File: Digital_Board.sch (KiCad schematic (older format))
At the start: 0 parts

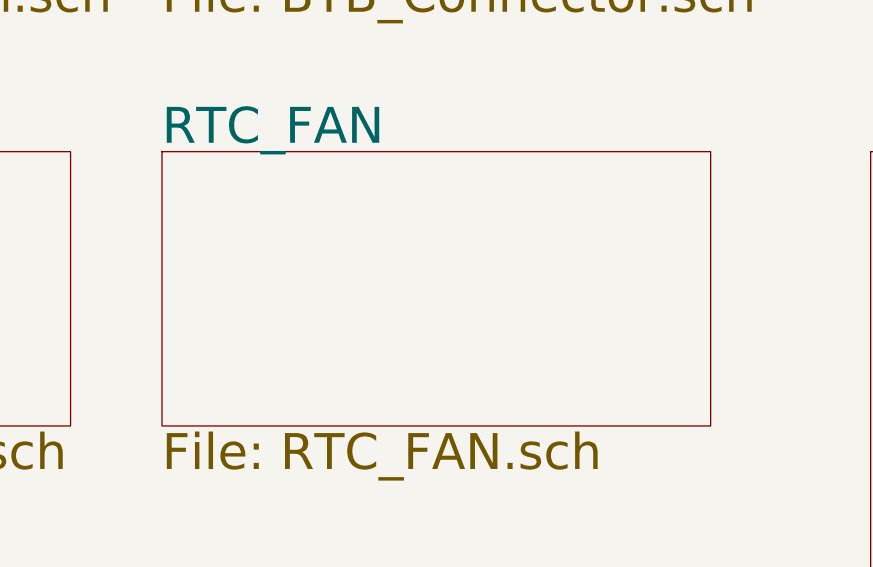
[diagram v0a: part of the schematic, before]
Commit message: Added new sheet for Ethernet PHY Connector and drawn schematic (continue)
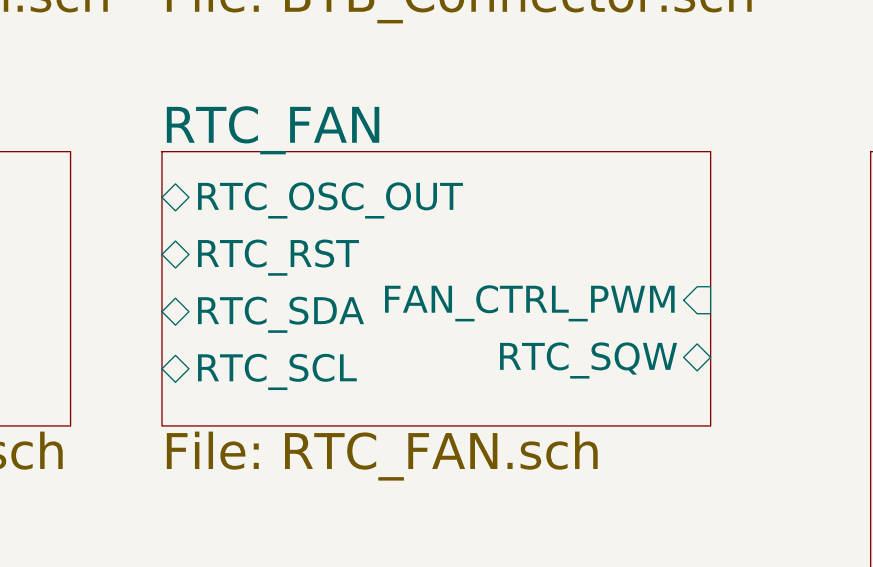
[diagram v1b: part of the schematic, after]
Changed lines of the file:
@@
 $Descr A2 23386 16535
 encoding utf-8
-Sheet 1 14
+Sheet 1 15
 Title "CGMPCX1006"
 Date "2021-02-03"
@@
 F0 "RTC_FAN" 157
 F1 "RTC_FAN.sch" 157
+F2 "RTC_SCL" B L 13900 4650 118
+F3 "RTC_SDA" B L 13900 4400 118
+F4 "RTC_RST" B L 13900 4150 118
+F5 "RTC_OSC_OUT" B L 13900 3900 118
+F6 "RTC_SQW" B R 16300 4600 118
+F7 "FAN_CTRL_PWM" I R 16300 4350 118
 $EndSheet
 $Sheet

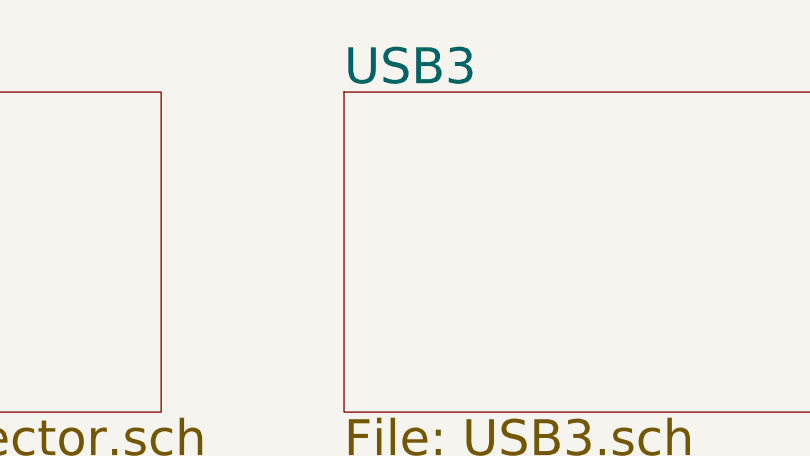
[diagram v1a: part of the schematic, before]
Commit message: Added USB SRAM sheet,Added USB3 ethernet ic
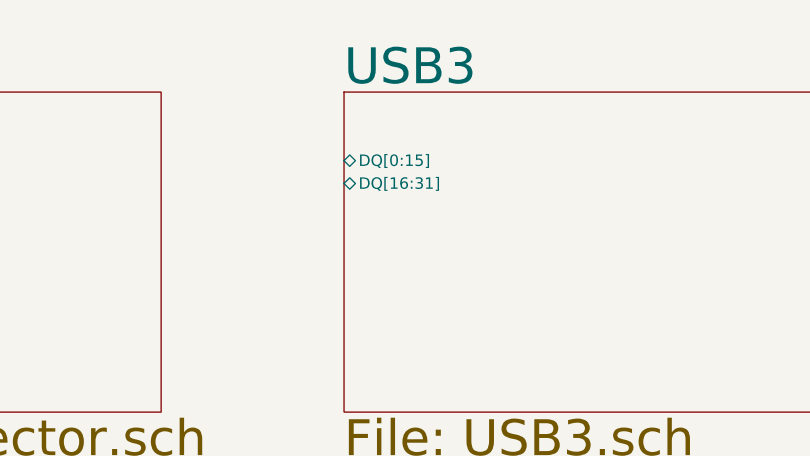
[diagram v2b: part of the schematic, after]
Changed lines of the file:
@@
 $Descr A2 23386 16535
 encoding utf-8
-Sheet 1 15
+Sheet 1 17
 Title "CGMPCX1006"
 Date "2021-02-03"
@@
 F0 "USB3" 157
 F1 "USB3.sch" 157
+F2 "DQ[0:15]" B L 17100 1800 50
+F3 "DQ[16:31]" B L 17100 1900 50
 $EndSheet
 $Sheet

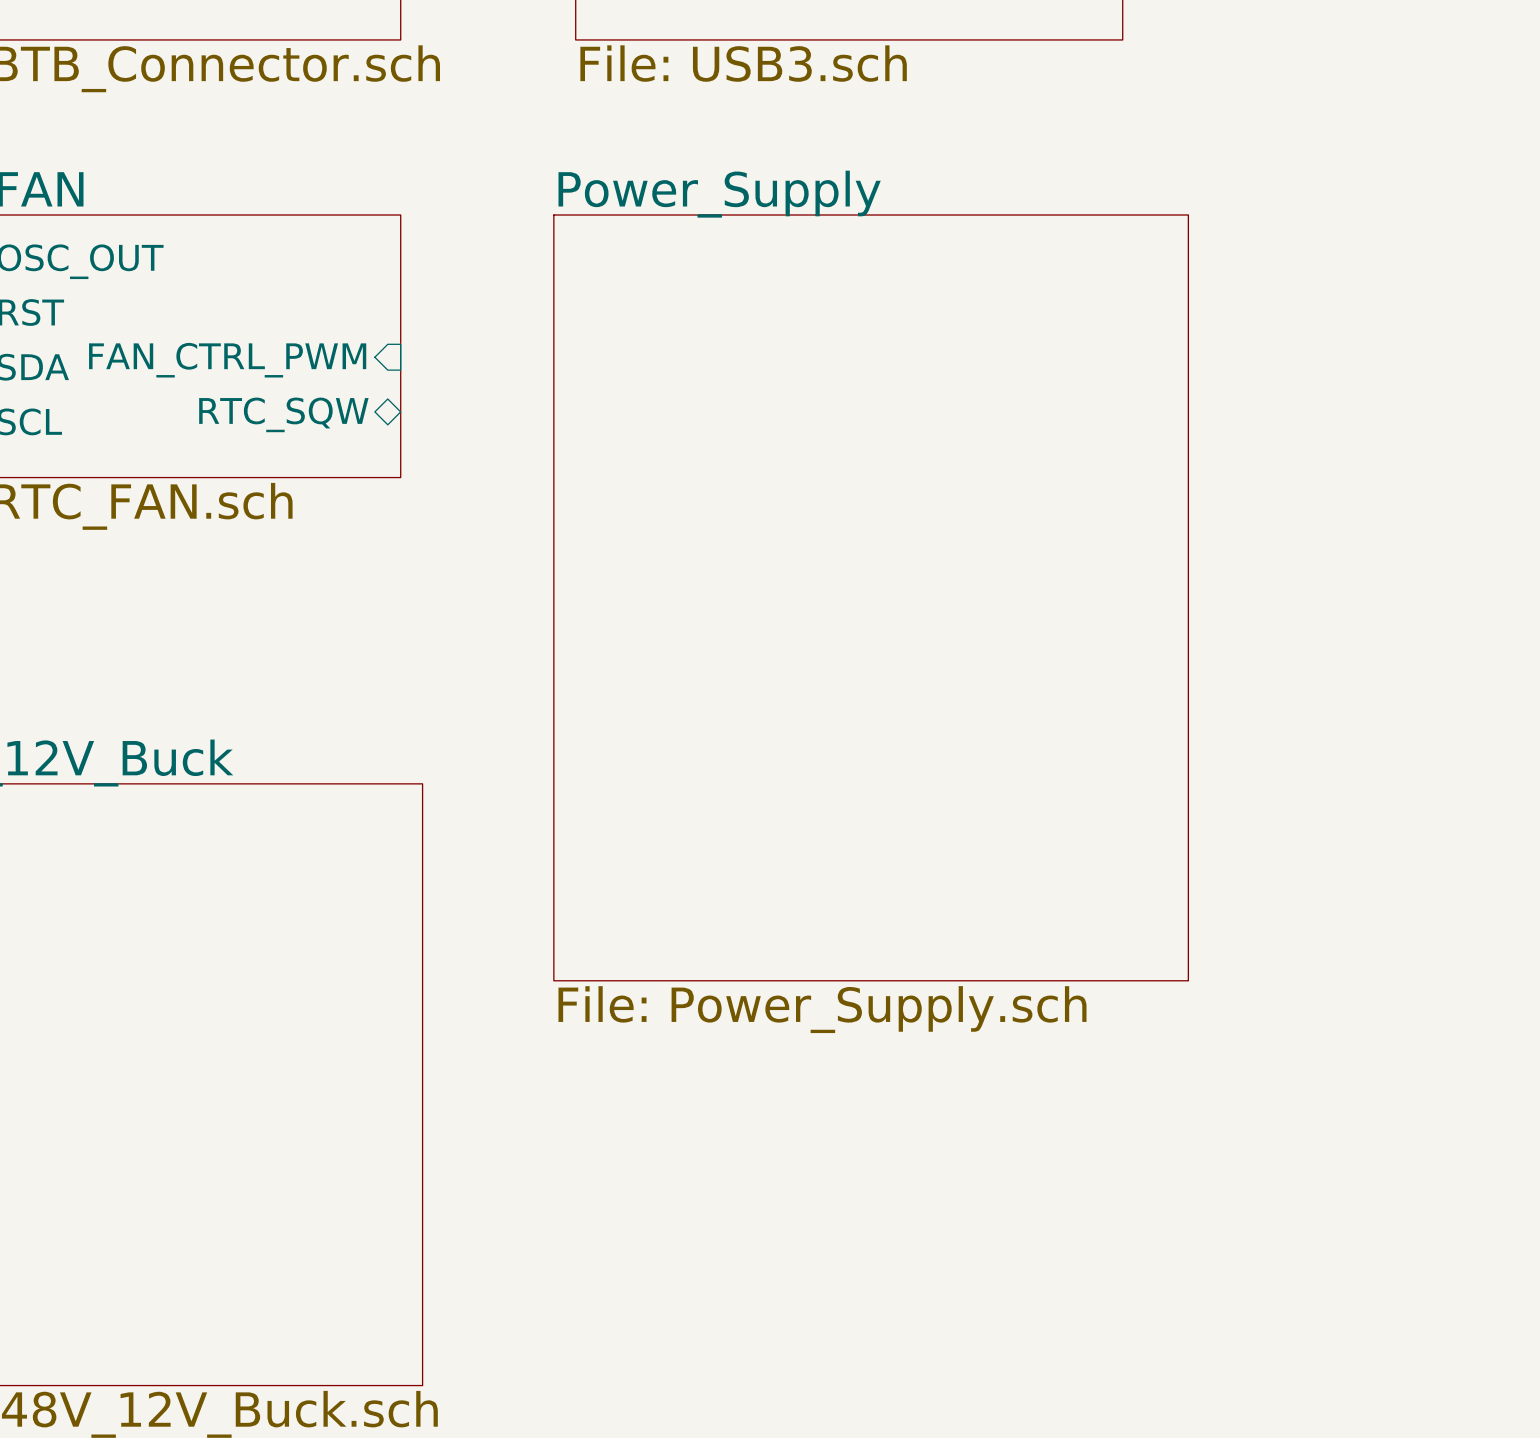
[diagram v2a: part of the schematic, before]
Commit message: Completed power 48v to 12v sheet
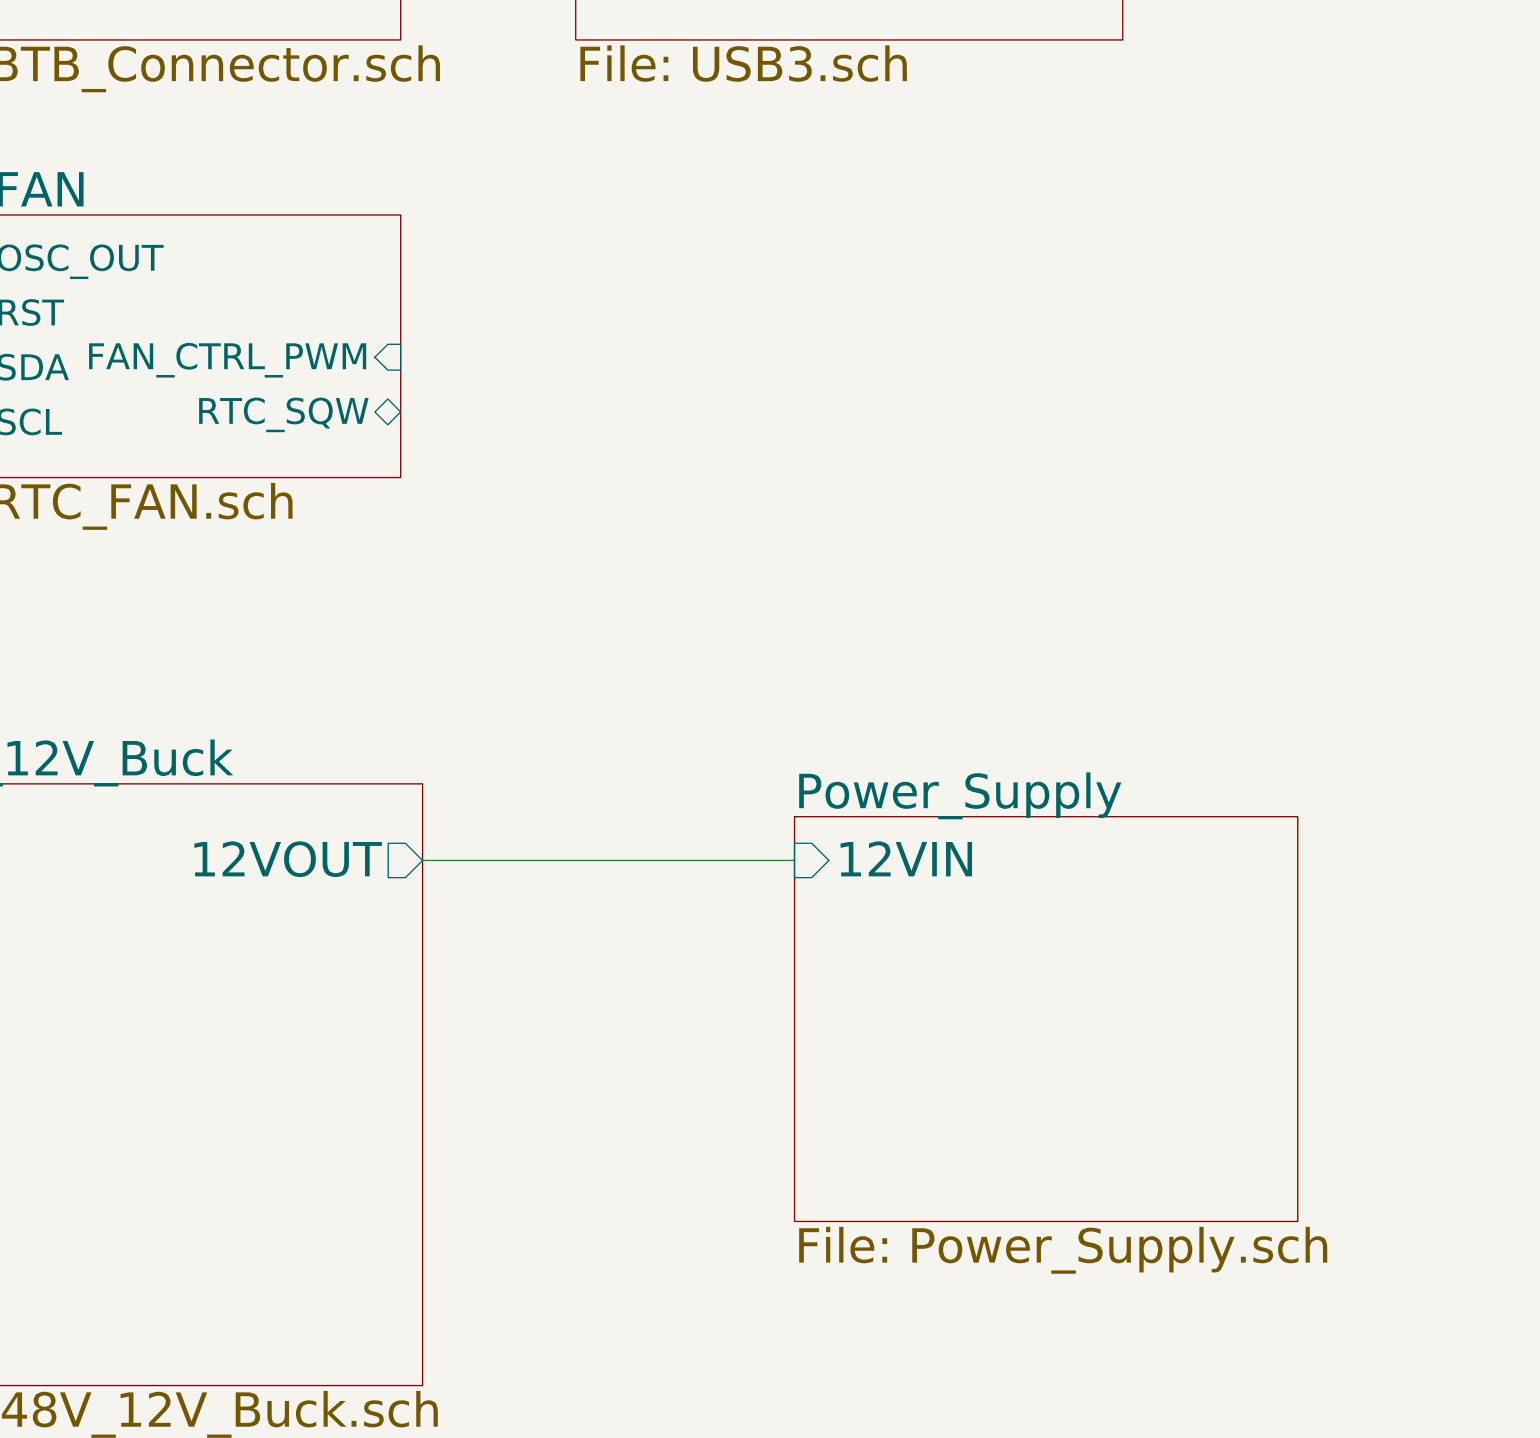
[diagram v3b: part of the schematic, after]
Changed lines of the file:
@@
 $EndSheet
 $Sheet
-S 17000 3700 2900 3500
+S 18100 6450 2300 1850
 U 601DF0A6
 F0 "Power_Supply" 157
 F1 "Power_Supply.sch" 157
+F2 "12VIN" I L 18100 6650 157
 $EndSheet
 $Sheet
@@
 F0 "48V_12V_Buck" 157
 F1 "48V_12V_Buck.sch" 157
+F2 "12VOUT" O R 16400 6650 157
 $EndSheet
+Wire Wire Line
+	16400 6650 18100 6650
 $EndSCHEMATC

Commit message: Completed USB3 1.2V Added 5V regulator cct partially completed Added BTB connector
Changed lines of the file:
@@
 $Descr A2 23386 16535
 encoding utf-8
-Sheet 1 17
+Sheet 1 18
 Title "CGMPCX1006"
 Date "2021-02-03"
@@
 $EndSheet
 $Sheet
-S 18100 6450 2300 1850
+S 5850 12700 2600 750
 U 601DF0A6
 F0 "Power_Supply" 157
 F1 "Power_Supply.sch" 157
-F2 "12VIN" I L 18100 6650 157
+F2 "12VIN" I L 5850 12900 157
 $EndSheet
 $Sheet
-S 13950 6300 2450 2750
+S 1750 12550 2450 900
 U 60256C5F
 F0 "48V_12V_Buck" 157
 F1 "48V_12V_Buck.sch" 157
-F2 "12VOUT" O R 16400 6650 157
+F2 "12VOUT" O R 4200 12900 157
 $EndSheet
 Wire Wire Line
-	16400 6650 18100 6650
+	4200 12900 5850 12900
+$Sheet
+S 2550 5850 2750 1550
+U 60318A5B
+F0 "BNC_trigger" 157
+F1 "BNC_Trigger.sch" 157
+$EndSheet
 $EndSCHEMATC

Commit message: Added sheet Ext_Analog
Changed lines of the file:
@@
-$EndSheet
-$Sheet
-S 17100 1500 2500 1400
-U 601E7BBE
-F0 "USB3" 157
-F1 "USB3.sch" 157
-F2 "DQ[0:15]" B L 17100 1800 50
-F3 "DQ[16:31]" B L 17100 1900 50
 $EndSheet
 $Sheet
@@
 $EndSheet
 $Sheet
-S 5500 3700 2800 1200
+S 17250 12000 2800 1200
 U 601E7C1E
 F0 "Comm_Interface" 157
@@
 $EndSheet
 $Sheet
-S 8800 3700 2300 1200
+S 17250 9950 2300 1200
 U 601E7C5A
 F0 "EEPROM" 157
@@
 $EndSheet
 $Sheet
-S 11600 3700 1900 1200
+S 17250 8150 1900 1200
 U 601E7C92
 F0 "Ethernet" 157
@@
 $EndSheet
 $Sheet
-S 13900 3700 2400 1200
+S 17100 4050 2400 1200
 U 601E7CC8
 F0 "RTC_FAN" 157
 F1 "RTC_FAN.sch" 157
-F2 "RTC_SCL" B L 13900 4650 118
-F3 "RTC_SDA" B L 13900 4400 118
-F4 "RTC_RST" B L 13900 4150 118
-F5 "RTC_OSC_OUT" B L 13900 3900 118
-F6 "RTC_SQW" B R 16300 4600 118
-F7 "FAN_CTRL_PWM" I R 16300 4350 118
+F2 "RTC_SCL" B L 17100 5000 118
+F3 "RTC_SDA" B L 17100 4750 118
+F4 "RTC_RST" B L 17100 4500 118
+F5 "RTC_OSC_OUT" B L 17100 4250 118
+F6 "RTC_SQW" B R 19500 4950 118
+F7 "FAN_CTRL_PWM" I R 19500 4700 118
 $EndSheet
 $Sheet
@@
 	4200 12900 5850 12900
 $Sheet
-S 2550 5850 2750 1550
+S 17100 1500 1000 1750
+U 601E7BBE
+F0 "USB3" 157
+F1 "USB3.sch" 157
+F2 "DQ[0:15]" B L 17100 1800 50
+F3 "DQ[16:31]" B L 17100 1900 50
+$EndSheet
+$Sheet
+S 17300 7300 1550 400
 U 60318A5B
-F0 "BNC_trigger" 157
-F1 "BNC_Trigger.sch" 157
+F0 "Ext_Analog" 157
+F1 "Ext_Analog.sch" 157
+F2 "BNC_TRIG_OUT" O L 17300 7500 50
 $EndSheet
 $EndSCHEMATC

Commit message: Completed LED_Comm Completed Ext_Analog Added AWG and ADC sheets
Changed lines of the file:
@@
 $Descr A2 23386 16535
 encoding utf-8
-Sheet 1 18
+Sheet 1 19
 Title "CGMPCX1006"
 Date "2021-02-03"
@@
 F0 "USB2" 157
 F1 "USB2.sch" 157
-$EndSheet
-$Sheet
-S 17250 12000 2800 1200
-U 601E7C1E
-F0 "Comm_Interface" 157
-F1 "Comm_Interface.sch" 157
 $EndSheet
 $Sheet
@@
 $EndSheet
 $Sheet
-S 17300 7300 1550 400
+S 17100 6350 1600 850
 U 60318A5B
 F0 "Ext_Analog" 157
 F1 "Ext_Analog.sch" 157
-F2 "BNC_TRIG_OUT" O L 17300 7500 50
+F2 "BNC_TRIG_OUT" O L 17100 6550 50
+F3 "AN0_P" O L 17100 6700 50
+F4 "AN0_N" O L 17100 6800 50
+F5 "AN1_P" O L 17100 6900 50
+F6 "AN1_N" O L 17100 7000 50
+$EndSheet
+$Sheet
+S 17100 12000 1000 2200
+U 601E7C1E
+F0 "LED_Comm" 157
+F1 "LED_Comm.sch" 157
+F2 "F_UART_TX" I L 17100 12200 50
+F3 "F_UART_RX" O L 17100 12300 50
+F4 "F_UART_SDA" B L 17100 12500 50
+F5 "F_UART_SCL" I L 17100 12600 50
+F6 "F_CAN_H" B L 17100 12800 50
+F7 "F_CAN_L" B L 17100 12900 50
+F8 "F_SPI_MISO" O L 17100 13100 50
+F9 "F_SPI_MOSI" I L 17100 13200 50
+F10 "F_SPI_CLK" I L 17100 13300 50
+F11 "F_SPI_SS" I L 17100 13400 50
+F12 "F_LCD_RESET" I L 17100 13600 50
+F13 "F_LCD_TX" I L 17100 13700 50
+F14 "F_LCD_RX" O L 17100 13800 50
+F15 "LED1" I L 17100 14000 50
+$EndSheet
+$Sheet
+S 1600 6500 2300 2100
+U 605FD9FD
+F0 "AWG" 50
+F1 "AWG.sch" 50
+$EndSheet
+$Sheet
+S 1600 9200 2300 1900
+U 605FDA0D
+F0 "ADC" 50
+F1 "ADC.sch" 50
 $EndSheet
 $EndSCHEMATC

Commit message: Added bus lines -ETH_PHY_CONN -RAM -USB2 Made Output the port direction of clkout of Clock_Gen Placed sheet entris of sheet symbols on top sheet
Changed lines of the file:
@@
 $Descr A2 23386 16535
 encoding utf-8
-Sheet 1 19
+Sheet 1 20
 Title "CGMPCX1006"
 Date "2021-02-03"
@@
 $EndSheet
 $Sheet
-S 8800 1500 2300 1400
-U 601E7AEB
-F0 "RAM" 157
-F1 "RAM.sch" 157
-$EndSheet
-$Sheet
 S 11600 1500 1900 1400
 U 601E7B38
 F0 "Clock_Gen" 157
 F1 "Clock_Gen.sch" 157
+F2 "CLK_IN0_P" I L 11600 1600 50
+F3 "CLK_IN0_N" I L 11600 1700 50
+F4 "CLK_IN1_P" I L 11600 1800 50
+F5 "CLK_IN1_N" I L 11600 1900 50
+F6 "CLK_IN2_P" I L 11600 2000 50
+F7 "CLK_IN2_N" I L 11600 2100 50
+F8 "CLK_IN3_P" I L 11600 2200 50
+F9 "CLK_IN3_N" I L 11600 2300 50
+F10 "CG_SDA" B R 13500 2700 50
+F11 "CG_SCL" B R 13500 2800 50
+F12 "CLK_OUT0_N" O R 13500 1650 50
+F13 "CLK_OUT0_P" O R 13500 1550 50
+F14 "CLK_OUT1_N" O R 13500 1850 50
+F15 "CLK_OUT1_P" O R 13500 1750 50
+F16 "CLK_OUT2_N" O R 13500 2050 50
+F17 "CLK_OUT2_P" O R 13500 1950 50
+F18 "CLK_OUT3_N" O R 13500 2250 50
+F19 "CLK_OUT3_P" O R 13500 2150 50
+F20 "CG_IN_SEL0" I R 13500 2400 50
+F21 "CG_IN_SEL1" I R 13500 2500 50
+F22 "CG_LOLB" O L 11600 2600 50
+F23 "CG_INTRB" O L 11600 2700 50
+F24 "CG_RSTB" I L 11600 2500 50
+F25 "CG_OEB" I L 11600 2800 50
 $EndSheet
 $Sheet
@@
 $EndSheet
 $Sheet
-S 2500 3700 1800 1100
+S 2150 4450 1500 850
 U 601E7BF0
 F0 "USB2" 157
 F1 "USB2.sch" 157
+F2 "USB2_DATA[0..7]" B R 3650 4650 50
+F3 "USB2_DIR" B R 3650 5100 50
+F4 "USB2_STP" B R 3650 5000 50
+F5 "USB2_NXT" B R 3650 4900 50
+F6 "USB2_RESTN" B R 3650 4800 50
+F7 "USB2_CLK" B R 3650 4550 50
+F8 "USB2_OC" B R 3650 5200 50
 $EndSheet
 $Sheet
@@
 F0 "EEPROM" 157
 F1 "EEPROM.sch" 157
+F2 "EEPROM_WC" I L 17250 10050 50
+F3 "EEPROM_SDA" I L 17250 10150 50
+F4 "EEPROM_SCL" I L 17250 10250 50
 $EndSheet
 $Sheet
@@
 F0 "Ethernet" 157
 F1 "Ethernet.sch" 157
+F2 "ETH_GPIO" I L 17250 8250 50
+F3 "ETH_JTAG_CLK" B L 17250 8400 50
+F4 "ETH_JTAG_TDI" B L 17250 8500 50
+F5 "ETH_JTAG_TDO" B L 17250 8600 50
+F6 "ETH_JTAG_TMS" B L 17250 8700 50
+F7 "ETH_MDC" I L 17250 8850 50
+F8 "ETH_MDIO" B L 17250 8950 50
+F9 "ETH_TX_CLK" I L 17250 9100 50
+F10 "ETH_TX_CTRL" I L 17250 9200 50
+F11 "ETH_TX_[0..3]" I L 17250 9300 50
+F12 "ETH_RX_[0..3]" I R 19150 9250 50
+F13 "ETH_RX_CLK" I R 19150 9150 50
+F14 "ETH_RX_CTRL" I R 19150 9050 50
 $EndSheet
 $Sheet
@@
 F1 "ADC.sch" 50
 $EndSheet
+$Sheet
+S 9250 1500 1550 3050
+U 601E7AEB
+F0 "RAM" 157
+F1 "RAM.sch" 157
+F2 "DDR3_CK_P" I R 10800 1600 50
+F3 "DDR3_CK_N" I R 10800 1700 50
+F4 "DDR3_CKE0" I R 10800 1900 50
+F5 "DDR3_CS" I R 10800 2000 50
+F6 "DDR3_RAS" I R 10800 2100 50
+F7 "DDR3_CAS" I R 10800 2200 50
+F8 "DDR3_WE" I R 10800 2300 50
+F9 "DDR3_BA[0..2]" I R 10800 2600 50
+F10 "DDR3_A[0..14]" I R 10800 2500 50
+F11 "DDR3_VREF" B R 10800 2750 50
+F12 "DDR3_RESET" I R 10800 2850 50
+F13 "DDR3_ODT0" I R 10800 2950 50
+F14 "DDR3_DM1" I R 10800 3050 50
+F15 "DDR3_DM0" I R 10800 3150 50
+F16 "DDR3_DM3" I R 10800 3250 50
+F17 "DDR3_DM2" I R 10800 3350 50
+F18 "DDR3_DQS0_N" B R 10800 3450 50
+F19 "DDR3_DQS0_P" B R 10800 3550 50
+F20 "DDR3_DQS1_N" B R 10800 3650 50
+F21 "DDR3_DQS1_P" B R 10800 3750 50
+F22 "DDR3_DQS2_N" B R 10800 3850 50
+F23 "DDR3_DQS2_P" B R 10800 3950 50
+F24 "DDR3_DQS3_N" B R 10800 4050 50
+F25 "DDR3_DQS3_P" B R 10800 4150 50
+F26 "DDR3_D[0..15]" B R 10800 4350 50
+F27 "DDR3_D[16..31]" B R 10800 4450 50
+$EndSheet
 $EndSCHEMATC
